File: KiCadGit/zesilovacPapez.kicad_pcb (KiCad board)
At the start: 2 copper layers, 141.2 x 141.2 mm, 81 parts, among them P1 CONN_01X01, P10 BNC, P11 CONN_01X01, P12 CONN_01X01, P13 BNC, P2 CONN_01X01, P3 CONN_01X01, P4 CONN_01X01, P5 CONN_01X01, P6 BNC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

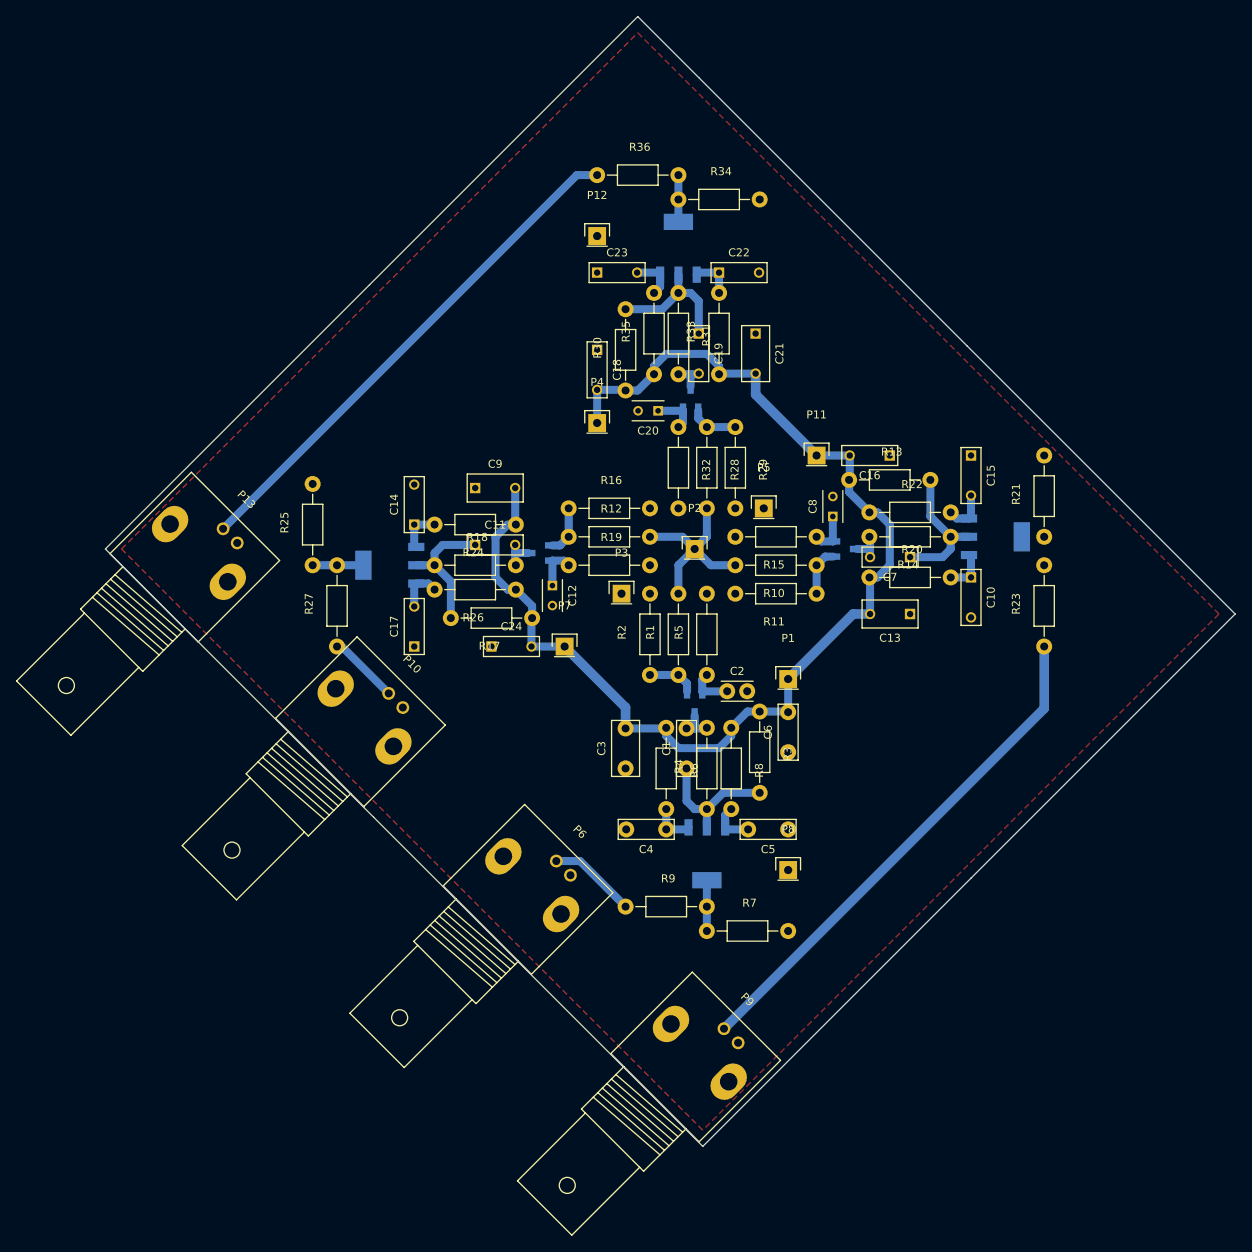
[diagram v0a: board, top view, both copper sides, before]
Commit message: Finalni verze RF zesilovace pred vyrobou. Upraveny dleky privodu, popisy a velikosti plosek.
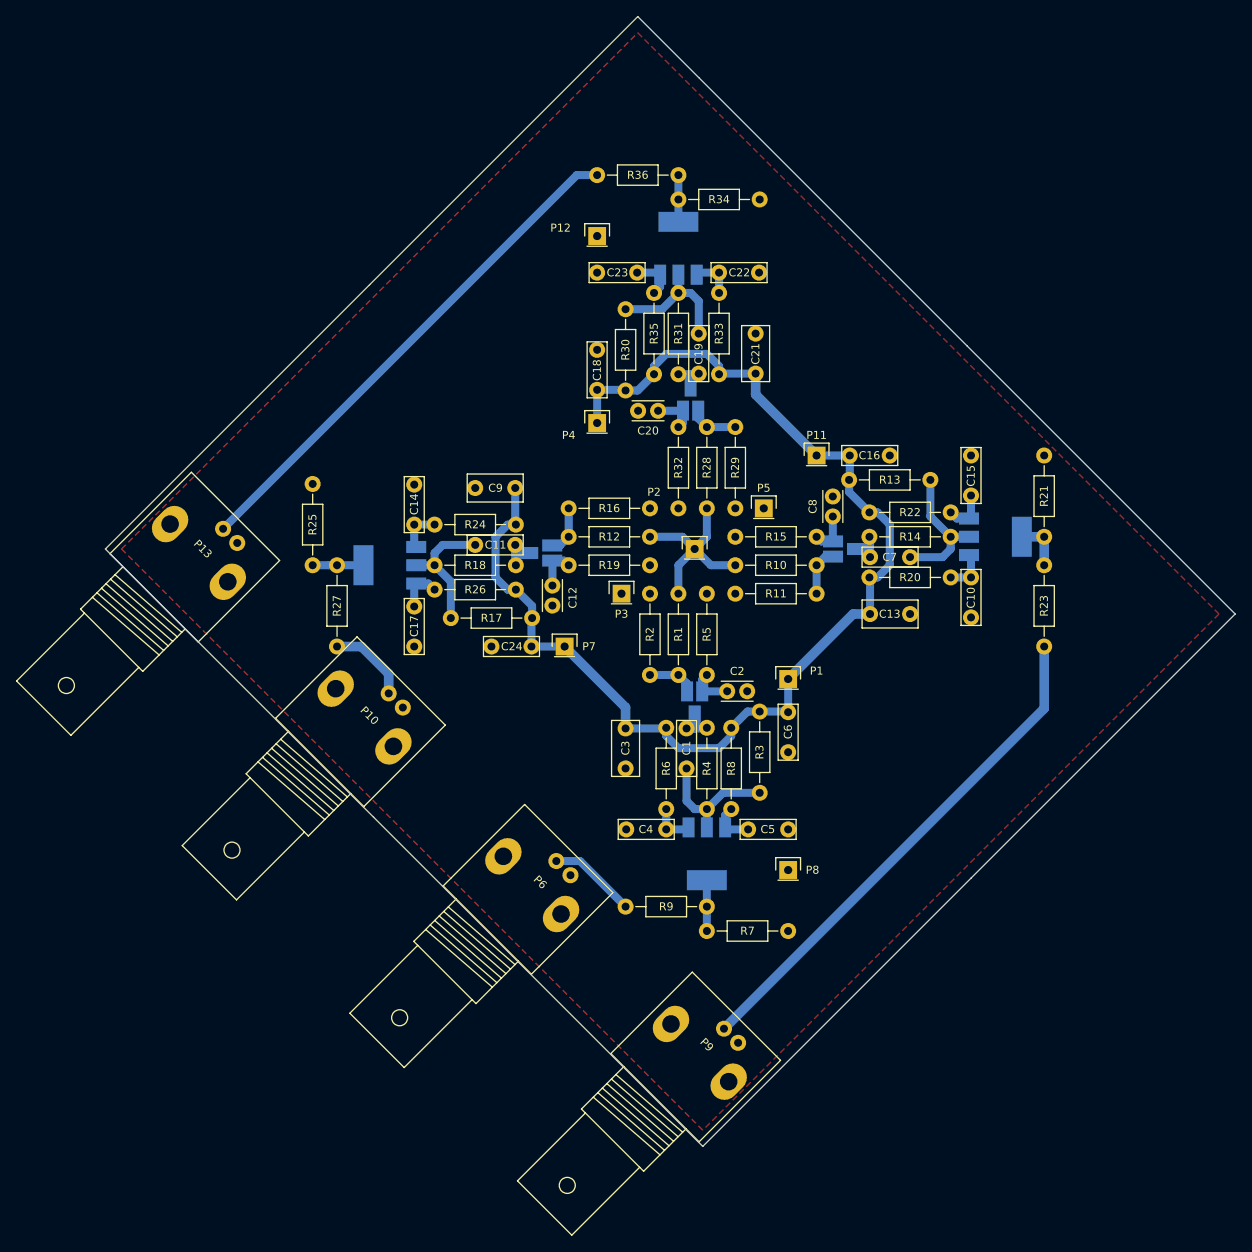
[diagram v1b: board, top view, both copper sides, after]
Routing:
- net Net-(Q5-Pad4): track 0.00 -> 6.35 mm
- net Net-(P10-Pad1): track 8.89 -> 10.3 mm

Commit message: DPS zesilovac: -upraveny diry na 0,8 mm pro kohouta a zvetseny centrealni a zemnici otvory pro privod kabelu.
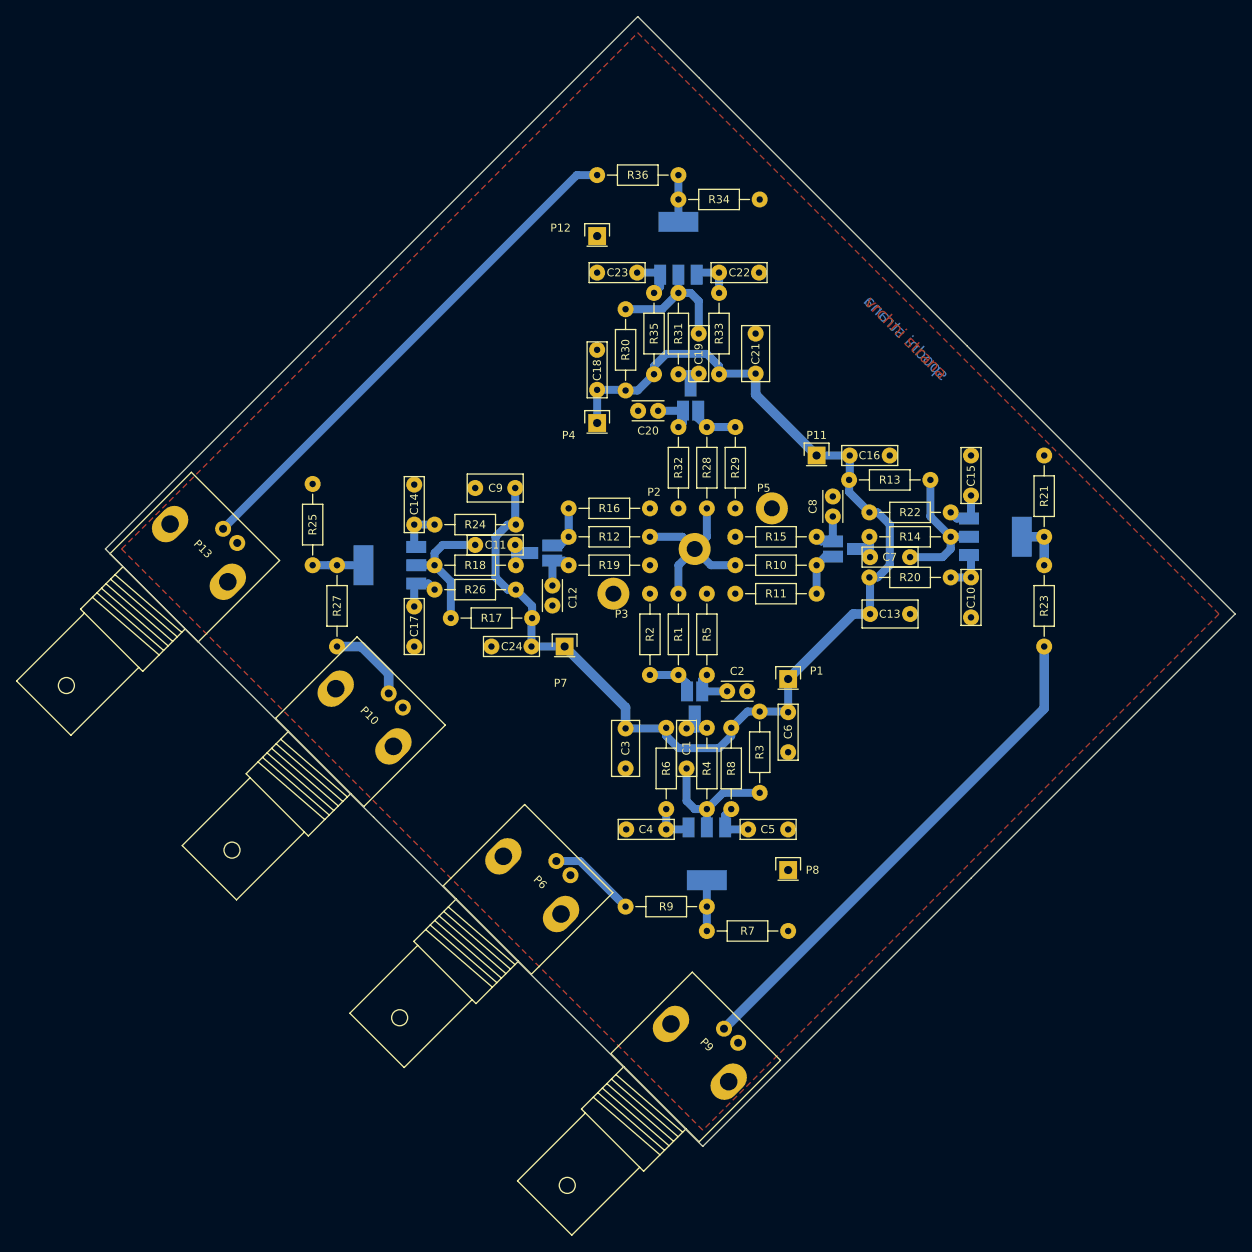
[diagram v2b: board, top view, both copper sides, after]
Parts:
- P1, P11, P4, P7: value CONN_01X01 -> VDD
- P12, P3, P5, P8: value CONN_01X01 -> GND
- P2: value CONN_01X01 -> INPUT
- moved P3 1.02 mm to (131.6, 90.4)
- moved P5 1.02 mm to (151.4, 79.8)
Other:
- board text added: "spodni strana"
- board text added: "vrchni strana"
